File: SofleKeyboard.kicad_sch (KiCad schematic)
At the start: 85 parts, among them J3 OLED, SW1 SW_PUSH_LED, SW10 SW_PUSH_LED, SW11 SW_PUSH_LED, SW12 SW_PUSH_LED, SW13 SW_PUSH_LED, SW14 SW_PUSH_LED, SW15 SW_PUSH_LED, SW16 SW_PUSH_LED, SW17 SW_PUSH_LED, SW18 SW_PUSH_LED, SW19 SW_PUSH_LED, SW2 SW_PUSH_LED, SW20 SW_PUSH_LED, SW21 SW_PUSH_LED, SW22 SW_PUSH_LED, SW23 SW_PUSH_LED, SW24 SW_PUSH_LED, SW25 SW_PUSH_LED, SW26 SW_PUSH_LED, SW27 SW_PUSH_LED, SW28 SW_PUSH_LED, SW29 SW_PUSH_LED, SW3 SW_PUSH_LED, SW30 SW_PUSH_LED, SW31 Rotary_Encoder_Switch, SW4 SW_PUSH_LED, SW5 SW_PUSH_LED, SW6 SW_PUSH_LED, SW7 SW_PUSH_LED, SW8 SW_PUSH_LED, SW9 SW_PUSH_LED, U1 ProMicro

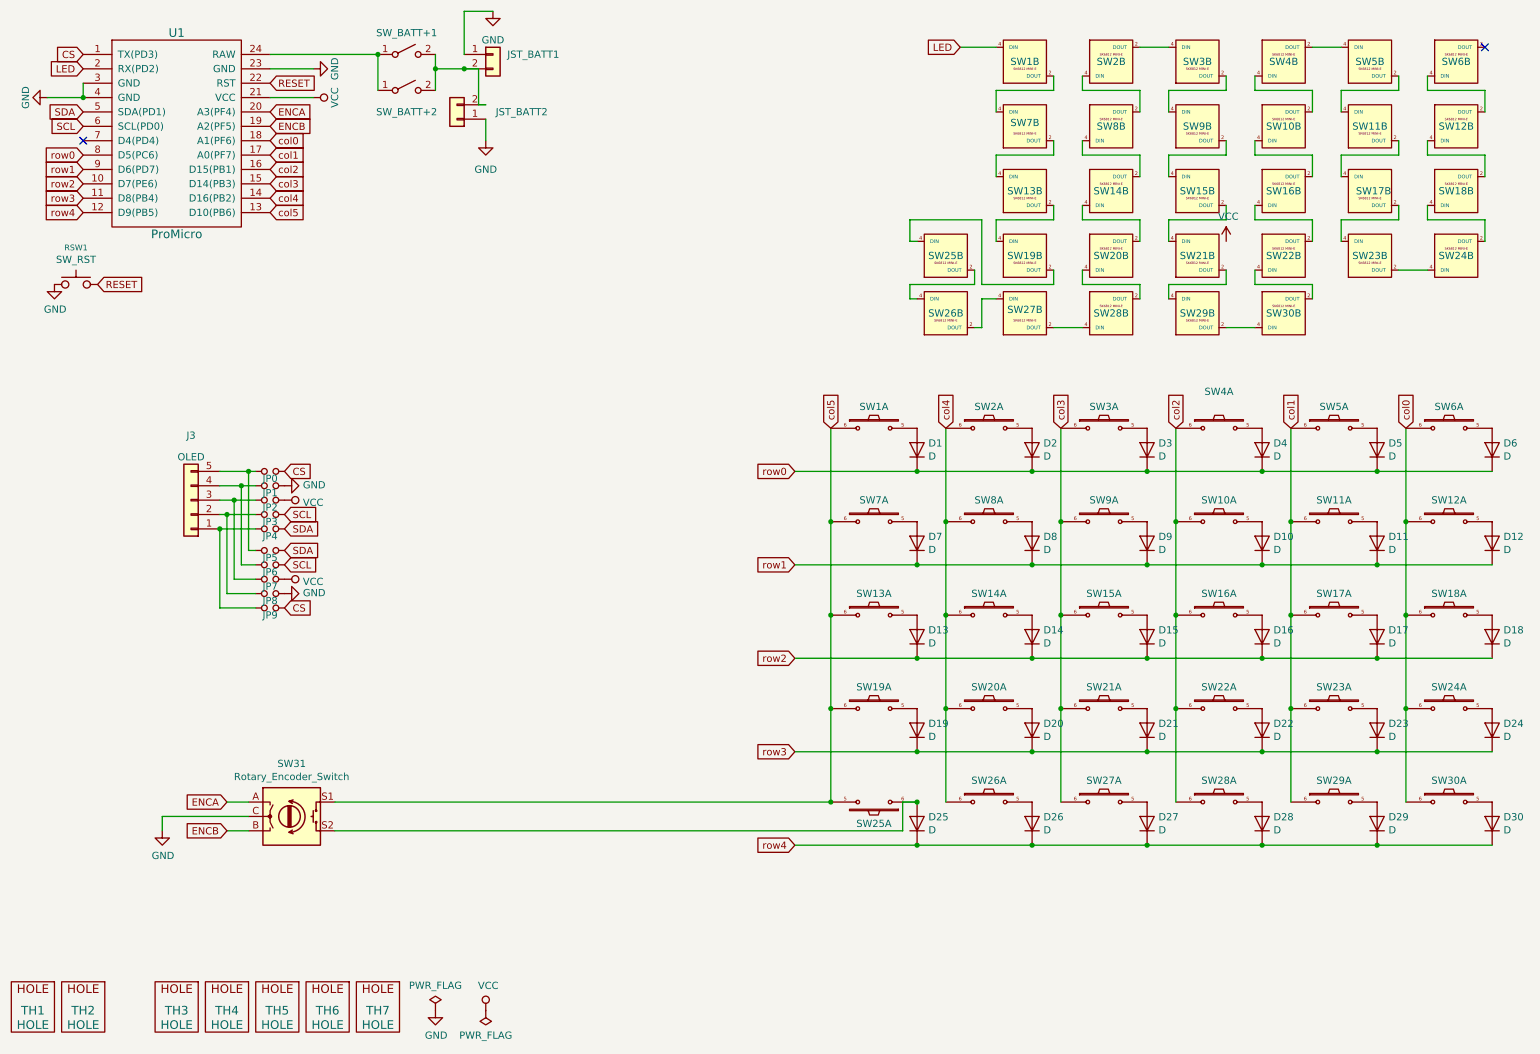
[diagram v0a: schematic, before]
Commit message: first stage: schematic and pcb footprints
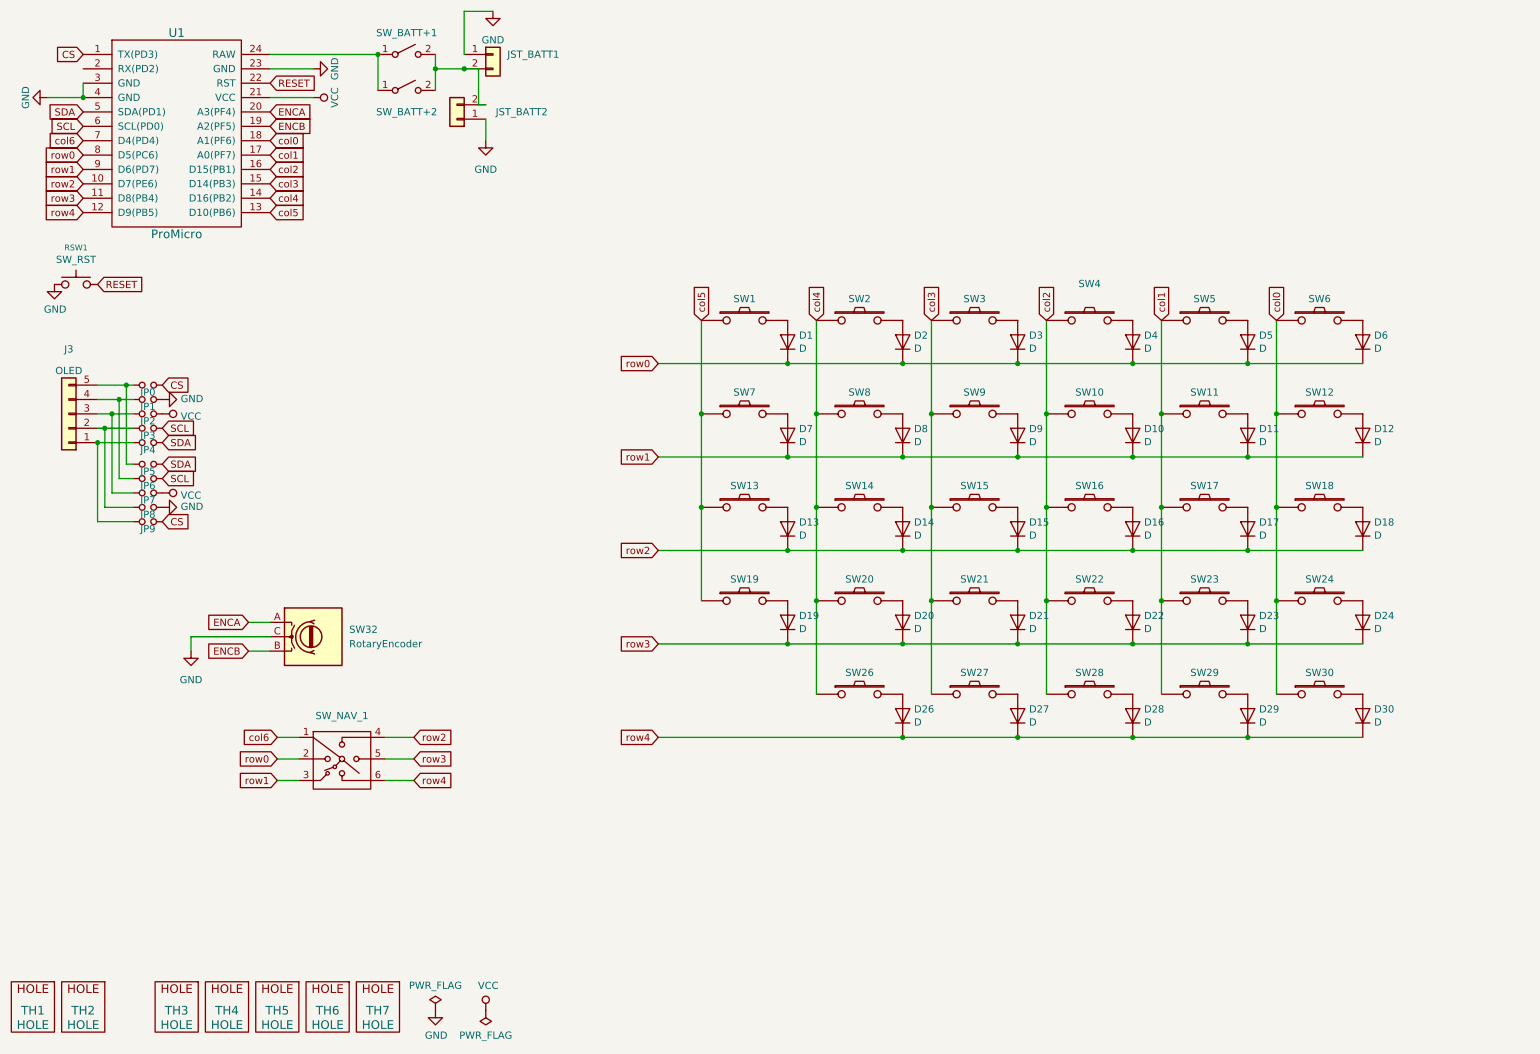
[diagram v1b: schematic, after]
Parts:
- removed D25: D, Diode_SMD:crkbd-diode, symbol SofleKeyboard-rescue:D-Lily58-cache-Lily58_Pro-rescue
- removed unit 2 of SW1
- removed unit 2 of SW10
- removed unit 2 of SW11
- removed unit 2 of SW12
- removed unit 2 of SW13
- removed unit 2 of SW14
- removed unit 2 of SW15
- removed unit 2 of SW16
- removed unit 2 of SW17
- removed unit 2 of SW18
- removed unit 2 of SW19
- removed unit 2 of SW2
- removed unit 2 of SW20
- removed unit 2 of SW21
- removed unit 2 of SW22
- removed unit 2 of SW23
- removed unit 2 of SW24
- removed SW25: SW_PUSH_LED, SofleChoc:Kailh-PG1350-1u-reversible-SK6812MiniE_MODIFIED, symbol SofleKeyboard:SW_PUSH_LED
- removed unit 2 of SW26
- removed unit 2 of SW27
- removed unit 2 of SW28
- removed unit 2 of SW29
- removed unit 2 of SW3
- removed unit 2 of SW30
- removed SW31: Rotary_Encoder_Switch, SofleKeyboard-footprint:RotaryEncoder_Alps_EC11E-Switch_Vertical_H20mm-keebio_modified, symbol Device:RotaryEncoder_Switch
- removed unit 2 of SW4
- removed unit 2 of SW5
- removed unit 2 of SW6
- removed unit 2 of SW7
- removed unit 2 of SW8
- removed unit 2 of SW9
- added SW32: RotaryEncoder, symbol Device:RotaryEncoder
- added SW_NAV_1: ~, symbol VicoKeyboard:SW_NAV_5
- SW1, SW13, SW19, SW7: footprint SofleChoc:Choc_Hotswap_SK6812MiniE_BiggerHSPads_Column1 -> VicoKeyboard:Choc_Hotswap_BiggerHSPads_Column1; symbol SofleKeyboard:SW_PUSH_LED -> VicoKeyboard:SW_PUSH_NOLED
- SW10, SW11, SW12, SW14, SW15, SW16, SW17, SW18, SW2, SW20, SW21, SW22, SW23, SW24, SW26, SW27, SW28, SW29, SW3, SW30, SW4, SW5, SW6, SW8, SW9: footprint SofleChoc:Choc_Hotswap_SK6812MiniE_BiggerHSPads -> VicoKeyboard:Choc_Hotswap_BiggerHSPads; symbol SofleKeyboard:SW_PUSH_LED -> VicoKeyboard:SW_PUSH_NOLED
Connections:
- net ENCA: now also SW32.A
- net ENCB: now also SW32.B
- net GND: now also SW32.C
- net col0: now also SW12.1, SW18.1, SW24.1, SW30.1, SW6.1; no longer SW12.6, SW18.6, SW24.6, SW30.6, SW6.6
- net col1: now also SW11.1, SW17.1, SW23.1, SW29.1, SW5.1; no longer SW11.6, SW17.6, SW23.6, SW29.6, SW5.6
- net col2: now also SW10.1, SW16.1, SW22.1, SW28.1, SW4.1; no longer SW10.6, SW16.6, SW22.6, SW28.6, SW4.6
- net col3: now also SW15.1, SW21.1, SW27.1, SW3.1, SW9.1; no longer SW15.6, SW21.6, SW27.6, SW3.6, SW9.6
- net col4: now also SW14.1, SW2.1, SW20.1, SW26.1, SW8.1; no longer SW14.6, SW2.6, SW20.6, SW26.6, SW8.6
- net col5: now also SW1.1, SW13.1, SW19.1, SW7.1; no longer SW1.6, SW13.6, SW19.6, SW7.6
- net row0: now also SW_NAV_1.2
- net row1: now also SW_NAV_1.3
- net row2: now also SW_NAV_1.4
- net row3: now also SW_NAV_1.5
- net row4: now also SW_NAV_1.6
- net col6: now reaches U1.7 (D4(PD4))
- net col6: now also SW_NAV_1.1
- net at D26.2 (A): now also SW26.2; no longer SW26.5
- net at D1.2 (A): now also SW1.2; no longer SW1.5
- net at D2.2 (A): now also SW2.2; no longer SW2.5
- net at D3.2 (A): now also SW3.2; no longer SW3.5
- net at D4.2 (A): now also SW4.2; no longer SW4.5
- net at D5.2 (A): now also SW5.2; no longer SW5.5
- net at D6.2 (A): now also SW6.2; no longer SW6.5
- net at D8.2 (A): now also SW8.2; no longer SW8.5
- net at D9.2 (A): now also SW9.2; no longer SW9.5
- net at D10.2 (A): now also SW10.2; no longer SW10.5
- net at D11.2 (A): now also SW11.2; no longer SW11.5
- net at D12.2 (A): now also SW12.2; no longer SW12.5
- net at D7.2 (A): now also SW7.2; no longer SW7.5
- net at D13.2 (A): now also SW13.2; no longer SW13.5
- net at D14.2 (A): now also SW14.2; no longer SW14.5
- net at D15.2 (A): now also SW15.2; no longer SW15.5
- net at D16.2 (A): now also SW16.2; no longer SW16.5
- net at D17.2 (A): now also SW17.2; no longer SW17.5
- net at D18.2 (A): now also SW18.2; no longer SW18.5
- net at D21.2 (A): now also SW21.2; no longer SW21.5
- net at D22.2 (A): now also SW22.2; no longer SW22.5
- net at D23.2 (A): now also SW23.2; no longer SW23.5
- net at D24.2 (A): now also SW24.2; no longer SW24.5
- net at D20.2 (A): now also SW20.2; no longer SW20.5
- net at D19.2 (A): now also SW19.2; no longer SW19.5
- net at D27.2 (A): now also SW27.2; no longer SW27.5
- net at D28.2 (A): now also SW28.2; no longer SW28.5
- net at D29.2 (A): now also SW29.2; no longer SW29.5
- net at D30.2 (A): now also SW30.2; no longer SW30.5
- net LED: no longer names the net of U1.2 (RX(PD2))
- no-connect marks 2 -> 0
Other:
- moved on the sheet: D1, D10, D11, D12, D13, D14, D15, D16, D17, D18, D19, D2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

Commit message: add sofle library, pcb outline, link new footprints to pcb
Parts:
- D1, D10, D11, D12, D13, D14, D15, D16, D17, D18, D19, D2, D20, D21, D22, D23, D24, D26, D27, D28, D29, D3, D30, D4, D5, D6, D7, D8, D9: footprint Diode_SMD:crkbd-diode -> Diode_SMD:D_SOD-123
- ENC1: renamed from SW32; footprint (none) -> Rotary_Encoder:RotaryEncoder_Alps_EC12E_Vertical_H20mm
- SW_NAV_1: value ~ -> SW_NAV; footprint (none) -> VicoKeyboard:NavSwitch_5Way
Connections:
- net col0: now also SW12.6, SW18.6, SW24.6, SW30.6, SW6.6; no longer SW12.1, SW18.1, SW24.1, SW30.1, SW6.1
- net col1: now also SW11.6, SW17.6, SW23.6, SW29.6, SW5.6; no longer SW11.1, SW17.1, SW23.1, SW29.1, SW5.1
- net col2: now also SW10.6, SW16.6, SW22.6, SW28.6, SW4.6; no longer SW10.1, SW16.1, SW22.1, SW28.1, SW4.1
- net col3: now also SW15.6, SW21.6, SW27.6, SW3.6, SW9.6; no longer SW15.1, SW21.1, SW27.1, SW3.1, SW9.1
- net col4: now also SW14.6, SW2.6, SW20.6, SW26.6, SW8.6; no longer SW14.1, SW2.1, SW20.1, SW26.1, SW8.1
- net col5: now also SW1.6, SW13.6, SW19.6, SW7.6; no longer SW1.1, SW13.1, SW19.1, SW7.1
- net at D26.2 (A): now also SW26.5; no longer SW26.2
- net at D1.2 (A): now also SW1.5; no longer SW1.2
- net at D2.2 (A): now also SW2.5; no longer SW2.2
- net at D3.2 (A): now also SW3.5; no longer SW3.2
- net at D4.2 (A): now also SW4.5; no longer SW4.2
- net at D5.2 (A): now also SW5.5; no longer SW5.2
- net at D6.2 (A): now also SW6.5; no longer SW6.2
- net at D8.2 (A): now also SW8.5; no longer SW8.2
- net at D9.2 (A): now also SW9.5; no longer SW9.2
- net at D10.2 (A): now also SW10.5; no longer SW10.2
- net at D11.2 (A): now also SW11.5; no longer SW11.2
- net at D12.2 (A): now also SW12.5; no longer SW12.2
- net at D7.2 (A): now also SW7.5; no longer SW7.2
- net at D13.2 (A): now also SW13.5; no longer SW13.2
- net at D14.2 (A): now also SW14.5; no longer SW14.2
- net at D15.2 (A): now also SW15.5; no longer SW15.2
- net at D16.2 (A): now also SW16.5; no longer SW16.2
- net at D17.2 (A): now also SW17.5; no longer SW17.2
- net at D18.2 (A): now also SW18.5; no longer SW18.2
- net at D21.2 (A): now also SW21.5; no longer SW21.2
- net at D22.2 (A): now also SW22.5; no longer SW22.2
- net at D23.2 (A): now also SW23.5; no longer SW23.2
- net at D24.2 (A): now also SW24.5; no longer SW24.2
- net at D20.2 (A): now also SW20.5; no longer SW20.2
- net at D19.2 (A): now also SW19.5; no longer SW19.2
- net at D27.2 (A): now also SW27.5; no longer SW27.2
- net at D28.2 (A): now also SW28.5; no longer SW28.2
- net at D29.2 (A): now also SW29.5; no longer SW29.2
- net at D30.2 (A): now also SW30.5; no longer SW30.2

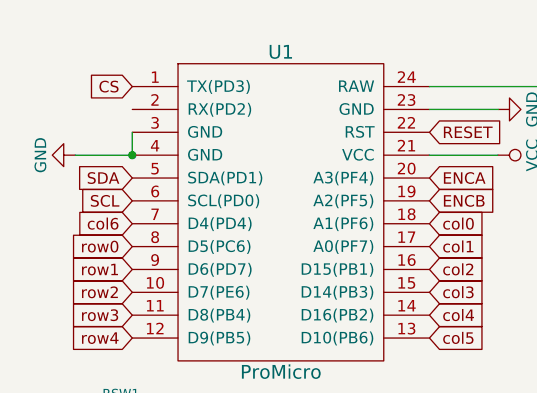
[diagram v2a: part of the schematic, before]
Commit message: update diode footprint, add ground zones, start board routing
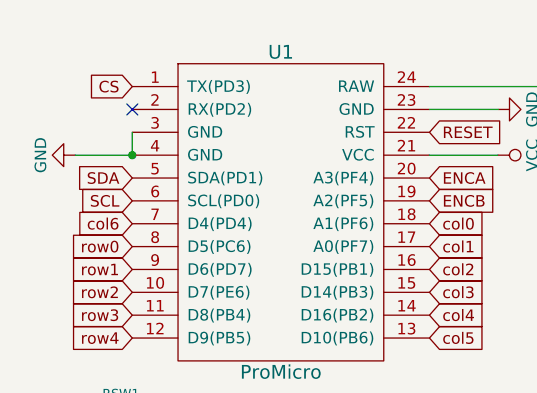
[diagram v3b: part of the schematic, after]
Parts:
- D1, D10, D11, D12, D13, D14, D15, D16, D17, D18, D19, D2, D20, D21, D22, D23, D24, D26, D27, D28, D29, D3, D30, D4, D5, D6, D7, D8, D9: footprint Diode_SMD:D_SOD-123 -> SofleChoc:crkbd-diode
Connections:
- no-connect marks 0 -> 1
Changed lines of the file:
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@@
 		(color 0 0 0 0)
 	)
+	(no_connect
+		(at 27.94 24.13)
+	)
 	(wire
 		(pts
@@
 			)
 		)
-		(property "Footprint" "Diode_SMD:D_SOD-123"
+		(property "Footprint" "SofleChoc:crkbd-diode"
 			(at 152.4 72.39 0)
 			(effects
@@
 			)
 		)
-		(property "Footprint" "Diode_SMD:D_SOD-123"
+		(property "Footprint" "SofleChoc:crkbd-diode"
 			(at 172.72 72.39 0)
 			(effects
@@
 			)
 		)
-		(property "Footprint" "Diode_SMD:D_SOD-123"
+		(property "Footprint" "SofleChoc:crkbd-diode"
 			(at 193.04 72.39 0)
 			(effects
@@
 			)
 		)
-		(property "Footprint" "Diode_SMD:D_SOD-123"
+		(property "Footprint" "SofleChoc:crkbd-diode"
 			(at 213.36 72.39 0)
 			(effects
@@
 			)
 		)
-		(property "Footprint" "Diode_SMD:D_SOD-123"
+		(property "Footprint" "SofleChoc:crkbd-diode"
 			(at 233.68 72.39 0)
 			(effects
@@
 			)
 		)
-		(property "Footprint" "Diode_SMD:D_SOD-123"
+		(property "Footprint" "SofleChoc:crkbd-diode"
 			(at 254 72.39 0)
 			(effects
@@
 			)
 		)
-		(property "Footprint" "Diode_SMD:D_SOD-123"
+		(property "Footprint" "SofleChoc:crkbd-diode"
 			(at 152.4 88.9 0)
 			(effects
@@
 			)
 		)
-		(property "Footprint" "Diode_SMD:D_SOD-123"
+		(property "Footprint" "SofleChoc:crkbd-diode"
 			(at 172.72 88.9 0)
 			(effects
@@
 			)
 		)
-		(property "Footprint" "Diode_SMD:D_SOD-123"
+		(property "Footprint" "SofleChoc:crkbd-diode"
 			(at 193.04 88.9 0)
 			(effects
@@
 			)
 		)
-		(property "Footprint" "Diode_SMD:D_SOD-123"
+		(property "Footprint" "SofleChoc:crkbd-diode"
 			(at 213.36 88.9 0)
 			(effects
@@
 			)
 		)
-		(property "Footprint" "Diode_SMD:D_SOD-123"
+		(property "Footprint" "SofleChoc:crkbd-diode"
 			(at 233.68 88.9 0)
 			(effects
@@
 			)
 		)
-		(property "Footprint" "Diode_SMD:D_SOD-123"
+		(property "Footprint" "SofleChoc:crkbd-diode"
 			(at 254 88.9 0)
 			(effects
@@
 			)
 		)
-		(property "Footprint" "Diode_SMD:D_SOD-123"
+		(property "Footprint" "SofleChoc:crkbd-diode"
 			(at 152.4 105.41 0)
 			(effects
@@
 			)
 		)
-		(property "Footprint" "Diode_SMD:D_SOD-123"
+		(property "Footprint" "SofleChoc:crkbd-diode"
 			(at 172.72 105.41 0)
 			(effects
@@
 			)
 		)
-		(property "Footprint" "Diode_SMD:D_SOD-123"
+		(property "Footprint" "SofleChoc:crkbd-diode"
 			(at 193.04 105.41 0)
 			(effects
@@
 			)
 		)
-		(property "Footprint" "Diode_SMD:D_SOD-123"
+		(property "Footprint" "SofleChoc:crkbd-diode"
 			(at 213.36 105.41 0)
 			(effects
@@
 			)
 		)
-		(property "Footprint" "Diode_SMD:D_SOD-123"
+		(property "Footprint" "SofleChoc:crkbd-diode"
 			(at 233.68 105.41 0)
 			(effects
@@
 			)
 		)
-		(property "Footprint" "Diode_SMD:D_SOD-123"
+		(property "Footprint" "SofleChoc:crkbd-diode"
 			(at 254 105.41 0)
 			(effects
@@
 			)
 		)
-		(property "Footprint" "Diode_SMD:D_SOD-123"
+		(property "Footprint" "SofleChoc:crkbd-diode"
 			(at 152.4 121.92 0)
 			(effects
@@
 			)
 		)
-		(property "Footprint" "Diode_SMD:D_SOD-123"
+		(property "Footprint" "SofleChoc:crkbd-diode"
 			(at 172.72 121.92 0)
 			(effects
@@
 			)
 		)
-		(property "Footprint" "Diode_SMD:D_SOD-123"
+		(property "Footprint" "SofleChoc:crkbd-diode"
 			(at 193.04 121.92 0)
 			(effects
@@
 			)
 		)
-		(property "Footprint" "Diode_SMD:D_SOD-123"
+		(property "Footprint" "SofleChoc:crkbd-diode"
 			(at 213.36 121.92 0)
 			(effects
@@
 			)
 		)
-		(property "Footprint" "Diode_SMD:D_SOD-123"
+		(property "Footprint" "SofleChoc:crkbd-diode"
 			(at 233.68 121.92 0)
 			(effects
@@
 			)
 		)
-		(property "Footprint" "Diode_SMD:D_SOD-123"
+		(property "Footprint" "SofleChoc:crkbd-diode"
 			(at 254 121.92 0)
 			(effects
@@
 			)
 		)
-		(property "Footprint" "Diode_SMD:D_SOD-123"
+		(property "Footprint" "SofleChoc:crkbd-diode"
 			(at 172.72 138.43 0)
 			(effects
@@
 			)
 		)
-		(property "Footprint" "Diode_SMD:D_SOD-123"
+		(property "Footprint" "SofleChoc:crkbd-diode"
 			(at 193.04 138.43 0)
 			(effects
@@
 			)
 		)
-		(property "Footprint" "Diode_SMD:D_SOD-123"
+		(property "Footprint" "SofleChoc:crkbd-diode"
 			(at 213.36 138.43 0)
 			(effects
@@
 			)
 		)
-		(property "Footprint" "Diode_SMD:D_SOD-123"
+		(property "Footprint" "SofleChoc:crkbd-diode"
 			(at 233.68 138.43 0)
 			(effects
@@
 			)
 		)
-		(property "Footprint" "Diode_SMD:D_SOD-123"
+		(property "Footprint" "SofleChoc:crkbd-diode"
 			(at 254 138.43 0)
 			(effects

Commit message: change pushbutton footprint, misc changes
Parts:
- removed JST_BATT2: Conn_01x02, SofleChoc:JST_PH_S2B-PH-K_1x02_P2.00mm_DoubleSided, symbol Connector_Generic:Conn_01x02
- RSW1: footprint SofleKeyboard-footprint:TACT_SWITCH_TVBP06 -> VicoKeyboard:Panasonic_EVQPUL_EVQPUC
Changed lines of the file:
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@@
 	(wire
 		(pts
-			(xy 97.79 30.48) (xy 99.06 30.48)
-		)
-		(stroke
-			(width 0)
-			(type default)
-		)
-	)
-	(wire
-		(pts
 			(xy 157.48 101.6) (xy 157.48 118.11)
 		)
@@
 	(wire
 		(pts
-			(xy 99.06 33.02) (xy 99.06 36.83)
-		)
-		(stroke
-			(width 0)
-			(type default)
-		)
-	)
-	(wire
-		(pts
 			(xy 33.02 85.09) (xy 33.02 99.06)
 		)
@@
 	(wire
 		(pts
-			(xy 97.79 30.48) (xy 97.79 24.13)
-		)
-		(stroke
-			(width 0)
-			(type default)
-		)
-	)
-	(wire
-		(pts
 			(xy 233.68 125.73) (xy 254 125.73)
 		)
@@
 			)
 		)
-		(property "Footprint" "SofleKeyboard-footprint:TACT_SWITCH_TVBP06"
+		(property "Footprint" "VicoKeyboard:Panasonic_EVQPUL_EVQPUC"
 			(at 26.67 62.23 0)
 			(effects
@@
 	)
 	(symbol
-		(lib_id "Connector_Generic:Conn_01x02")
-		(at 93.98 33.02 180)
-		(unit 1)
-		(exclude_from_sim no)
-		(in_bom yes)
-		(on_board yes)
-		(dnp no)
-		(property "Reference" "JST_BATT2"
-			(at 105.41 31.75 0)
-			(effects
-				(font
-					(size 1.27 1.27)
-				)
-			)
-		)
-		(property "Value" "Conn_01x02"
-			(at 91.44 30.4801 0)
-			(effects
-				(font
-					(size 1.27 1.27)
-				)
-				(justify left)
-				(hide yes)
-			)
-		)
-		(property "Footprint" "SofleChoc:JST_PH_S2B-PH-K_1x02_P2.00mm_DoubleSided"
-			(at 93.98 33.02 0)
-			(effects
-				(font
-					(size 1.27 1.27)
-				)
-				(hide yes)
-			)
-		)
-		(property "Datasheet" "~"
-			(at 93.98 33.02 0)
-			(effects
-				(font
-					(size 1.27 1.27)
-				)
-				(hide yes)
-			)
-		)
-		(property "Description" ""
-			(at 93.98 33.02 0)
-			(effects
-				(font
-					(size 1.27 1.27)
-				)
-			)
-		)
-		(pin "1"
-		)
-		(pin "2"
-		)
-		(instances
-			(project ""
-				(path "/43cfd488-4c9d-4da2-b703-dd4909c44cb8"
-					(reference "JST_BATT2")
-					(unit 1)
-				)
-			)
-		)
-	)
-	(symbol
 		(lib_id "SofleKeyboard-rescue:Jumper_NO_Small-Device")
 		(at 39.37 82.55 0)
@@
 					(unit 1)
 				)
-			)
-		)
-	)
-	(symbol
-		(lib_id "power:GND")
-		(at 99.06 36.83 0)
-		(unit 1)
-		(exclude_from_sim no)
-		(in_bom yes)
-		(on_board yes)
-		(dnp no)
-		(fields_autoplaced yes)
-		(property "Reference" "#PWR0110"
-			(at 99.06 43.18 0)
-			(effects
-				(font
-					(size 1.27 1.27)
-				)
-				(hide yes)
-			)
-		)
-		(property "Value" "GND"
-			(at 99.06 41.91 0)
-			(effects
-				(font
-					(size 1.27 1.27)
-				)
-			)
-		)
-		(property "Footprint" ""
-			(at 99.06 36.83 0)
-			(effects
-				(font
-					(size 1.27 1.27)
-				)
-				(hide yes)
-			)
-		)
-		(property "Datasheet" ""
-			(at 99.06 36.83 0)
-			(effects
-				(font
-					(size 1.27 1.27)
-				)
-				(hide yes)
-			)
-		)
-		(property "Description" ""
-			(at 99.06 36.83 0)
-			(effects
-				(font
-					(size 1.27 1.27)
-				)
-			)
-		)
-		(pin "1"
-		)
-		(instances
-			(project ""
-				(path "/43cfd488-4c9d-4da2-b703-dd4909c44cb8"
-					(reference "#PWR0110")
-					(unit 1)
-				)
